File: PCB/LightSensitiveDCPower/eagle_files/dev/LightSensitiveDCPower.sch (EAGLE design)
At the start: 5 parts, among them SW1 PCM12SMTR

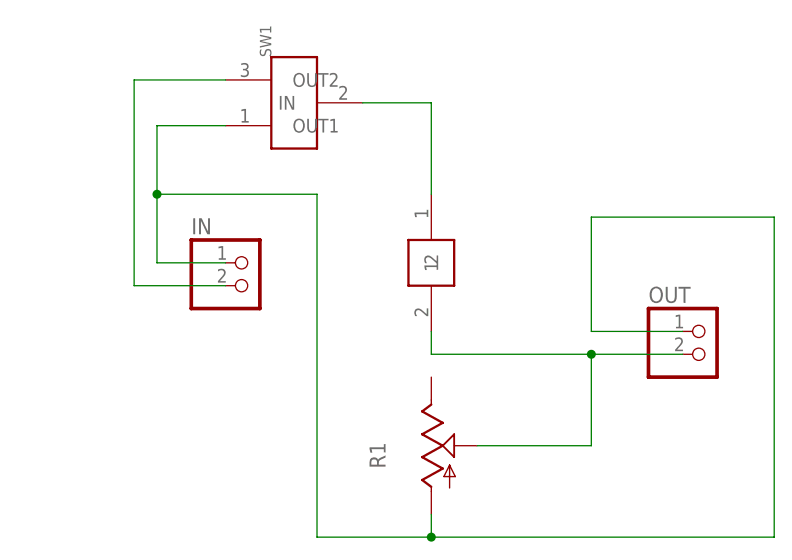
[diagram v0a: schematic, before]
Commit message: New horizontal female header scheme for Light Sensitive DC power with dimensions adjusted accordingly.
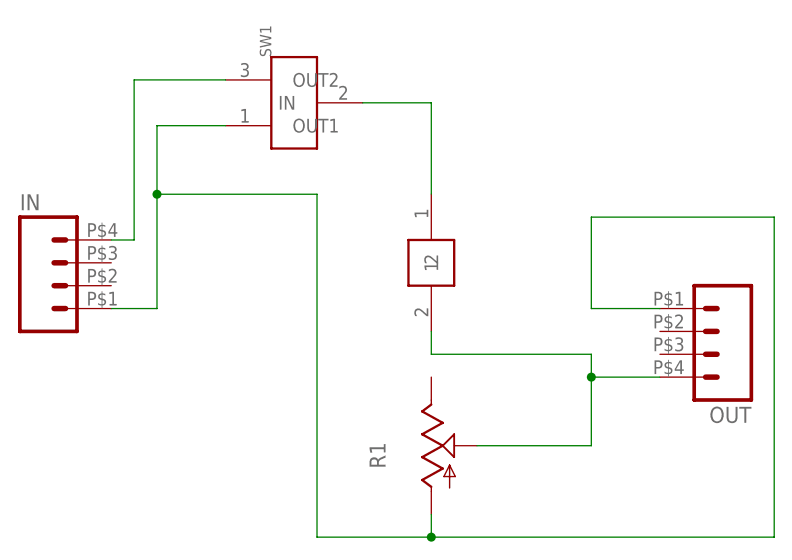
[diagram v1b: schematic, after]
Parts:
- IN, OUT: device pinhead:PINHD-1X2 -> SparkFun-Connectors:M04HORIZ_PTH
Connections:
- net N$2: now also IN.4; no longer IN.2
- net N$4: now also OUT.4; no longer OUT.2
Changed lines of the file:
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@@
 <?xml version="1.0" encoding="utf-8"?>
 <!DOCTYPE eagle SYSTEM "eagle.dtd">
-<eagle version="7.1.0">
+<eagle version="7.2.0">
 <drawing>
 <settings>
@@
 <layer number="48" name="Document" color="7" fill="1" visible="no" active="no"/>
 <layer number="49" name="Reference" color="7" fill="1" visible="no" active="no"/>
+<layer number="50" name="dxf" color="7" fill="1" visible="no" active="no"/>
 <layer number="51" name="tDocu" color="7" fill="1" visible="no" active="no"/>
 <layer number="52" name="bDocu" color="7" fill="1" visible="no" active="no"/>
+<layer number="53" name="tGND_GNDA" color="7" fill="9" visible="no" active="no"/>
+<layer number="54" name="bGND_GNDA" color="1" fill="9" visible="no" active="no"/>
+<layer number="56" name="wert" color="7" fill="1" visible="no" active="no"/>
 <layer number="90" name="Modules" color="5" fill="1" visible="yes" active="yes"/>
 <layer number="91" name="Nets" color="2" fill="1" visible="yes" active="yes"/>
@@
 <layer number="97" name="Info" color="7" fill="1" visible="yes" active="yes"/>
 <layer number="98" name="Guide" color="6" fill="1" visible="yes" active="yes"/>
+<layer number="100" name="Muster" color="7" fill="1" visible="no" active="no"/>
+<layer number="101" name="Patch_Top" color="12" fill="4" visible="yes" active="yes"/>
+<layer number="102" name="Vscore" color="7" fill="1" visible="yes" active="yes"/>
+<layer number="103" name="tMap" color="7" fill="1" visible="yes" active="yes"/>
+<layer number="104" name="Name" color="16" fill="1" visible="yes" active="yes"/>
+<layer number="105" name="tPlate" color="7" fill="1" visible="yes" active="yes"/>
+<layer number="106" name="bPlate" color="7" fill="1" visible="yes" active="yes"/>
+<layer number="107" name="Crop" color="7" fill="1" visible="yes" active="yes"/>
+<layer number="108" name="tplace-old" color="10" fill="1" visible="yes" active="yes"/>
+<layer number="109" name="ref-old" color="11" fill="1" visible="yes" active="yes"/>
+<layer number="116" name="Patch_BOT" color="9" fill="4" visible="yes" active="yes"/>
+<layer number="121" name="_tsilk" color="7" fill="1" visible="yes" active="yes"/>
+<layer number="122" name="_bsilk" color="7" fill="1" visible="yes" active="yes"/>
+<layer number="125" name="_tNames" color="7" fill="1" visible="yes" active="yes"/>
+<layer number="144" name="Drill_legend" color="7" fill="1" visible="yes" active="yes"/>
+<layer number="151" name="HeatSink" color="7" fill="1" visible="yes" active="yes"/>
+<layer number="199" name="Contour" color="7" fill="1" visible="yes" active="yes"/>
+<layer number="200" name="200bmp" color="1" fill="10" visible="yes" active="yes"/>
+<layer number="201" name="201bmp" color="2" fill="10" visible="yes" active="yes"/>
+<layer number="202" name="202bmp" color="3" fill="10" visible="yes" active="yes"/>
+<layer number="203" name="203bmp" color="4" fill="10" visible="yes" active="yes"/>
+<layer number="204" name="204bmp" color="5" fill="10" visible="yes" active="yes"/>
+<layer number="205" name="205bmp" color="6" fill="10" visible="yes" active="yes"/>
+<layer number="206" name="206bmp" color="7" fill="10" visible="yes" active="yes"/>
+<layer number="207" name="207bmp" color="8" fill="10" visible="yes" active="yes"/>
+<layer number="208" name="208bmp" color="9" fill="10" visible="yes" active="yes"/>
+<layer number="209" name="209bmp" color="7" fill="1" visible="yes" active="yes"/>
+<layer number="210" name="210bmp" color="7" fill="1" visible="yes" active="yes"/>
+<layer number="211" name="211bmp" color="7" fill="1" visible="yes" active="yes"/>
+<layer number="212" name="212bmp" color="7" fill="1" visible="yes" active="yes"/>
+<layer number="213" name="213bmp" color="7" fill="1" visible="yes" active="yes"/>
+<layer number="214" name="214bmp" color="7" fill="1" visible="yes" active="yes"/>
+<layer number="215" name="215bmp" color="7" fill="1" visible="yes" active="yes"/>
+<layer number="216" name="216bmp" color="7" fill="1" visible="yes" active="yes"/>
+<layer number="217" name="217bmp" color="18" fill="1" visible="no" active="no"/>
+<layer number="218" name="218bmp" color="19" fill="1" visible="no" active="no"/>
+<layer number="219" name="219bmp" color="20" fill="1" visible="no" active="no"/>
+<layer number="220" name="220bmp" color="21" fill="1" visible="no" active="no"/>
+<layer number="221" name="221bmp" color="22" fill="1" visible="no" active="no"/>
+<layer number="222" name="222bmp" color="23" fill="1" visible="no" active="no"/>
+<layer number="223" name="223bmp" color="24" fill="1" visible="no" active="no"/>
+<layer number="224" name="224bmp" color="25" fill="1" visible="no" active="no"/>
+<layer number="250" name="Descript" color="3" fill="1" visible="no" active="no"/>
+<layer number="251" name="SMDround" color="12" fill="11" visible="no" active="no"/>
+<layer number="254" name="cooling" color="7" fill="1" visible="yes" active="yes"/>
 </layers>
 <schematic xreflabel="%F%N/%S.%C%R" xrefpart="/%S.%C%R">
@@
 <part name="SW1" library="freddyLibr" deviceset="PCM12SMTR" device=""/>
 <part name="R1" library="pot" deviceset="TRIM_US-" device="B25P"/>
-<part name="IN" library="pinhead" deviceset="PINHD-1X2" device=""/>
-<part name="OUT" library="pinhead" deviceset="PINHD-1X2" device=""/>
+<part name="IN" library="SparkFun-Connectors" deviceset="M04" device="HORIZ_PTH"/>
+<part name="OUT" library="SparkFun-Connectors" deviceset="M04" device="HORIZ_PTH"/>
 </parts>
 <sheets>
@@
 <instance part="SW1" gate="G$1" x="-10.16" y="71.12" rot="R90"/>
 <instance part="R1" gate="G$1" x="5.08" y="33.02"/>
-<instance part="IN" gate="G$1" x="-15.24" y="50.8"/>
-<instance part="OUT" gate="G$1" x="35.56" y="43.18"/>
+<instance part="IN" gate="G$1" x="-35.56" y="50.8"/>
+<instance part="OUT" gate="G$1" x="35.56" y="45.72" rot="R180"/>
 </instances>
 <busses>
@@
 <net name="N$1" class="0">
 <segment>
-<pinref part="IN" gate="G$1" pin="1"/>
-<wire x1="-17.78" y1="53.34" x2="-25.4" y2="53.34" width="0.1524" layer="91"/>
-<wire x1="-25.4" y1="53.34" x2="-25.4" y2="60.96" width="0.1524" layer="91"/>
 <pinref part="SW1" gate="G$1" pin="OUT1"/>
 <wire x1="-25.4" y1="60.96" x2="-25.4" y2="68.58" width="0.1524" layer="91"/>
@@
 <wire x1="-7.62" y1="22.86" x2="-7.62" y2="60.96" width="0.1524" layer="91"/>
 <wire x1="-7.62" y1="60.96" x2="-25.4" y2="60.96" width="0.1524" layer="91"/>
-<junction x="-25.4" y="60.96"/>
-<pinref part="OUT" gate="G$1" pin="1"/>
-<wire x1="33.02" y1="45.72" x2="22.86" y2="45.72" width="0.1524" layer="91"/>
-<wire x1="22.86" y1="45.72" x2="22.86" y2="58.42" width="0.1524" layer="91"/>
+<wire x1="22.86" y1="48.26" x2="22.86" y2="58.42" width="0.1524" layer="91"/>
 <wire x1="22.86" y1="58.42" x2="43.18" y2="58.42" width="0.1524" layer="91"/>
 <wire x1="43.18" y1="58.42" x2="43.18" y2="22.86" width="0.1524" layer="91"/>
 <wire x1="43.18" y1="22.86" x2="5.08" y2="22.86" width="0.1524" layer="91"/>
 <junction x="5.08" y="22.86"/>
+<junction x="-25.4" y="60.96"/>
+<wire x1="-25.4" y1="60.96" x2="-25.4" y2="48.26" width="0.1524" layer="91"/>
+<pinref part="IN" gate="G$1" pin="1"/>
+<wire x1="-25.4" y1="48.26" x2="-30.48" y2="48.26" width="0.1524" layer="91"/>
+<pinref part="OUT" gate="G$1" pin="1"/>
+<wire x1="30.48" y1="48.26" x2="22.86" y2="48.26" width="0.1524" layer="91"/>
 </segment>
 </net>
 <net name="N$2" class="0">
 <segment>
-<pinref part="IN" gate="G$1" pin="2"/>
-<wire x1="-17.78" y1="50.8" x2="-27.94" y2="50.8" width="0.1524" layer="91"/>
-<wire x1="-27.94" y1="50.8" x2="-27.94" y2="73.66" width="0.1524" layer="91"/>
 <pinref part="SW1" gate="G$1" pin="OUT2"/>
 <wire x1="-27.94" y1="73.66" x2="-17.78" y2="73.66" width="0.1524" layer="91"/>
+<pinref part="IN" gate="G$1" pin="4"/>
+<wire x1="-30.48" y1="55.88" x2="-27.94" y2="55.88" width="0.1524" layer="91"/>
+<wire x1="-27.94" y1="55.88" x2="-27.94" y2="73.66" width="0.1524" layer="91"/>
 </segment>
 </net>
@@
 <pinref part="R1" gate="G$1" pin="S"/>
 <wire x1="10.16" y1="33.02" x2="22.86" y2="33.02" width="0.1524" layer="91"/>
-<wire x1="22.86" y1="33.02" x2="22.86" y2="43.18" width="0.1524" layer="91"/>
-<pinref part="OUT" gate="G$1" pin="2"/>
-<wire x1="22.86" y1="43.18" x2="33.02" y2="43.18" width="0.1524" layer="91"/>
+<wire x1="22.86" y1="33.02" x2="22.86" y2="40.64" width="0.1524" layer="91"/>
 <pinref part="PC1" gate="G$1" pin="2"/>
+<wire x1="22.86" y1="40.64" x2="22.86" y2="43.18" width="0.1524" layer="91"/>
 <wire x1="5.08" y1="45.72" x2="5.08" y2="43.18" width="0.1524" layer="91"/>
 <wire x1="5.08" y1="43.18" x2="22.86" y2="43.18" width="0.1524" layer="91"/>
-<junction x="22.86" y="43.18"/>
+<pinref part="OUT" gate="G$1" pin="4"/>
+<wire x1="30.48" y1="40.64" x2="22.86" y2="40.64" width="0.1524" layer="91"/>
+<junction x="22.86" y="40.64"/>
 </segment>
 </net>

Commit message: Removed switch. Intended use case turned out to be out of rating.
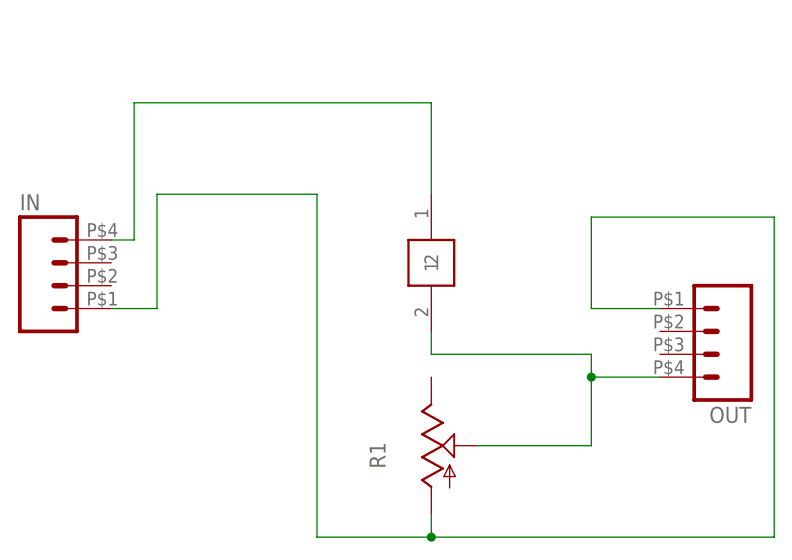
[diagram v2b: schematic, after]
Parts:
- removed SW1: PCM12SMTR, freddyLibr:PCM12SMTR
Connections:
- removed net N$3: PC1.1, SW1.IN
- net N$1: no longer SW1.OUT1
- net N$2: now also PC1.1; no longer SW1.OUT2
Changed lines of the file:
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@@
 <parts>
 <part name="PC1" library="freddyLibr" deviceset="PDV-P8101" device=""/>
-<part name="SW1" library="freddyLibr" deviceset="PCM12SMTR" device=""/>
 <part name="R1" library="pot" deviceset="TRIM_US-" device="B25P"/>
 <part name="IN" library="SparkFun-Connectors" deviceset="M04" device="HORIZ_PTH"/>
@@
 <instances>
 <instance part="PC1" gate="G$1" x="5.08" y="53.34"/>
-<instance part="SW1" gate="G$1" x="-10.16" y="71.12" rot="R90"/>
 <instance part="R1" gate="G$1" x="5.08" y="33.02"/>
 <instance part="IN" gate="G$1" x="-35.56" y="50.8"/>
@@
 <net name="N$1" class="0">
 <segment>
-<pinref part="SW1" gate="G$1" pin="OUT1"/>
-<wire x1="-25.4" y1="60.96" x2="-25.4" y2="68.58" width="0.1524" layer="91"/>
-<wire x1="-25.4" y1="68.58" x2="-17.78" y2="68.58" width="0.1524" layer="91"/>
 <pinref part="R1" gate="G$1" pin="A"/>
 <wire x1="5.08" y1="25.4" x2="5.08" y2="22.86" width="0.1524" layer="91"/>
@@
 <wire x1="43.18" y1="22.86" x2="5.08" y2="22.86" width="0.1524" layer="91"/>
 <junction x="5.08" y="22.86"/>
-<junction x="-25.4" y="60.96"/>
 <wire x1="-25.4" y1="60.96" x2="-25.4" y2="48.26" width="0.1524" layer="91"/>
 <pinref part="IN" gate="G$1" pin="1"/>
@@
 <net name="N$2" class="0">
 <segment>
-<pinref part="SW1" gate="G$1" pin="OUT2"/>
-<wire x1="-27.94" y1="73.66" x2="-17.78" y2="73.66" width="0.1524" layer="91"/>
 <pinref part="IN" gate="G$1" pin="4"/>
 <wire x1="-30.48" y1="55.88" x2="-27.94" y2="55.88" width="0.1524" layer="91"/>
-<wire x1="-27.94" y1="55.88" x2="-27.94" y2="73.66" width="0.1524" layer="91"/>
+<pinref part="PC1" gate="G$1" pin="1"/>
+<wire x1="5.08" y1="60.96" x2="5.08" y2="71.12" width="0.1524" layer="91"/>
+<wire x1="5.08" y1="71.12" x2="-27.94" y2="71.12" width="0.1524" layer="91"/>
+<wire x1="-27.94" y1="71.12" x2="-27.94" y2="55.88" width="0.1524" layer="91"/>
 </segment>
 </net>
-<net name="N$3" class="0">
-<segment>
-<pinref part="SW1" gate="G$1" pin="IN"/>
-<pinref part="PC1" gate="G$1" pin="1"/>
-<wire x1="-2.54" y1="71.12" x2="5.08" y2="71.12" width="0.1524" layer="91"/>
-<wire x1="5.08" y1="71.12" x2="5.08" y2="60.96" width="0.1524" layer="91"/>
-</segment>
-</net>

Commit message: LiSensiPow actually works now
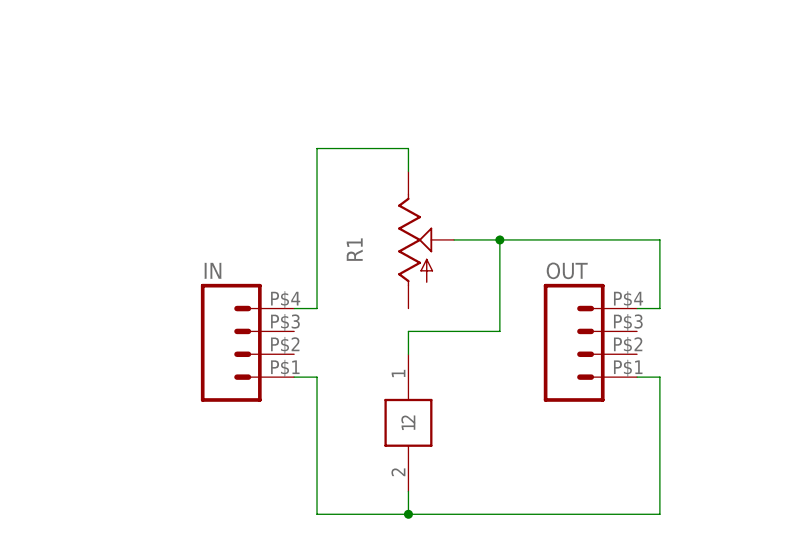
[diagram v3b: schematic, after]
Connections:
- removed net N$2: IN.4, PC1.1
- new net N$3: IN.4, R1.E
- net N$1: now also PC1.2; no longer R1.A
- net N$4: now also PC1.1; no longer PC1.2
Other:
- moved on the sheet: IN, OUT, R1
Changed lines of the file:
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@@
 </plain>
 <instances>
-<instance part="PC1" gate="G$1" x="5.08" y="53.34"/>
-<instance part="R1" gate="G$1" x="5.08" y="33.02"/>
-<instance part="IN" gate="G$1" x="-35.56" y="50.8"/>
-<instance part="OUT" gate="G$1" x="35.56" y="45.72" rot="R180"/>
+<instance part="PC1" gate="G$1" x="2.54" y="35.56"/>
+<instance part="R1" gate="G$1" x="2.54" y="55.88"/>
+<instance part="IN" gate="G$1" x="-15.24" y="43.18"/>
+<instance part="OUT" gate="G$1" x="22.86" y="43.18"/>
 </instances>
 <busses>
@@
 <net name="N$1" class="0">
 <segment>
-<pinref part="R1" gate="G$1" pin="A"/>
-<wire x1="5.08" y1="25.4" x2="5.08" y2="22.86" width="0.1524" layer="91"/>
-<wire x1="5.08" y1="22.86" x2="-7.62" y2="22.86" width="0.1524" layer="91"/>
-<wire x1="-7.62" y1="22.86" x2="-7.62" y2="60.96" width="0.1524" layer="91"/>
-<wire x1="-7.62" y1="60.96" x2="-25.4" y2="60.96" width="0.1524" layer="91"/>
-<wire x1="22.86" y1="48.26" x2="22.86" y2="58.42" width="0.1524" layer="91"/>
-<wire x1="22.86" y1="58.42" x2="43.18" y2="58.42" width="0.1524" layer="91"/>
-<wire x1="43.18" y1="58.42" x2="43.18" y2="22.86" width="0.1524" layer="91"/>
-<wire x1="43.18" y1="22.86" x2="5.08" y2="22.86" width="0.1524" layer="91"/>
-<junction x="5.08" y="22.86"/>
-<wire x1="-25.4" y1="60.96" x2="-25.4" y2="48.26" width="0.1524" layer="91"/>
 <pinref part="IN" gate="G$1" pin="1"/>
-<wire x1="-25.4" y1="48.26" x2="-30.48" y2="48.26" width="0.1524" layer="91"/>
+<wire x1="-10.16" y1="40.64" x2="-7.62" y2="40.64" width="0.1524" layer="91"/>
+<wire x1="-7.62" y1="40.64" x2="-7.62" y2="25.4" width="0.1524" layer="91"/>
+<pinref part="PC1" gate="G$1" pin="2"/>
+<wire x1="-7.62" y1="25.4" x2="2.54" y2="25.4" width="0.1524" layer="91"/>
+<wire x1="2.54" y1="25.4" x2="2.54" y2="27.94" width="0.1524" layer="91"/>
 <pinref part="OUT" gate="G$1" pin="1"/>
-<wire x1="30.48" y1="48.26" x2="22.86" y2="48.26" width="0.1524" layer="91"/>
+<wire x1="27.94" y1="40.64" x2="30.48" y2="40.64" width="0.1524" layer="91"/>
+<wire x1="30.48" y1="40.64" x2="30.48" y2="25.4" width="0.1524" layer="91"/>
+<wire x1="30.48" y1="25.4" x2="2.54" y2="25.4" width="0.1524" layer="91"/>
+<junction x="2.54" y="25.4"/>
 </segment>
 </net>
-<net name="N$2" class="0">
+<net name="N$3" class="0">
 <segment>
 <pinref part="IN" gate="G$1" pin="4"/>
-<wire x1="-30.48" y1="55.88" x2="-27.94" y2="55.88" width="0.1524" layer="91"/>
-<pinref part="PC1" gate="G$1" pin="1"/>
-<wire x1="5.08" y1="60.96" x2="5.08" y2="71.12" width="0.1524" layer="91"/>
-<wire x1="5.08" y1="71.12" x2="-27.94" y2="71.12" width="0.1524" layer="91"/>
-<wire x1="-27.94" y1="71.12" x2="-27.94" y2="55.88" width="0.1524" layer="91"/>
+<wire x1="-10.16" y1="48.26" x2="-7.62" y2="48.26" width="0.1524" layer="91"/>
+<wire x1="-7.62" y1="48.26" x2="-7.62" y2="66.04" width="0.1524" layer="91"/>
+<pinref part="R1" gate="G$1" pin="E"/>
+<wire x1="-7.62" y1="66.04" x2="2.54" y2="66.04" width="0.1524" layer="91"/>
+<wire x1="2.54" y1="66.04" x2="2.54" y2="63.5" width="0.1524" layer="91"/>
 </segment>
 </net>
@@
 <segment>
 <pinref part="R1" gate="G$1" pin="S"/>
-<wire x1="10.16" y1="33.02" x2="22.86" y2="33.02" width="0.1524" layer="91"/>
-<wire x1="22.86" y1="33.02" x2="22.86" y2="40.64" width="0.1524" layer="91"/>
-<pinref part="PC1" gate="G$1" pin="2"/>
-<wire x1="22.86" y1="40.64" x2="22.86" y2="43.18" width="0.1524" layer="91"/>
-<wire x1="5.08" y1="45.72" x2="5.08" y2="43.18" width="0.1524" layer="91"/>
-<wire x1="5.08" y1="43.18" x2="22.86" y2="43.18" width="0.1524" layer="91"/>
+<wire x1="7.62" y1="55.88" x2="12.7" y2="55.88" width="0.1524" layer="91"/>
+<wire x1="12.7" y1="55.88" x2="30.48" y2="55.88" width="0.1524" layer="91"/>
+<wire x1="30.48" y1="55.88" x2="30.48" y2="48.26" width="0.1524" layer="91"/>
 <pinref part="OUT" gate="G$1" pin="4"/>
-<wire x1="30.48" y1="40.64" x2="22.86" y2="40.64" width="0.1524" layer="91"/>
-<junction x="22.86" y="40.64"/>
+<wire x1="30.48" y1="48.26" x2="27.94" y2="48.26" width="0.1524" layer="91"/>
+<pinref part="PC1" gate="G$1" pin="1"/>
+<wire x1="2.54" y1="43.18" x2="2.54" y2="45.72" width="0.1524" layer="91"/>
+<wire x1="2.54" y1="45.72" x2="12.7" y2="45.72" width="0.1524" layer="91"/>
+<wire x1="12.7" y1="45.72" x2="12.7" y2="55.88" width="0.1524" layer="91"/>
+<junction x="12.7" y="55.88"/>
 </segment>
 </net>
